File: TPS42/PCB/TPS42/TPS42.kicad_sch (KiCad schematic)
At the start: 67 parts, among them J11 Conn_01x06, J3 TP Sensor Module, J4 TP Module, J5 Conn_01x02, J7 TrackPoint, J8 Battery, J9 TP Sensor Module, SW1 SW_DPST_x2, SW2 Reset, SW3 Reset, U1 ProMicro, U11 Hole, U12 Hole, U14 ProMicro, U4 Hole, U5 Hole, U7 Hole, U8 Hole, U9 Hole

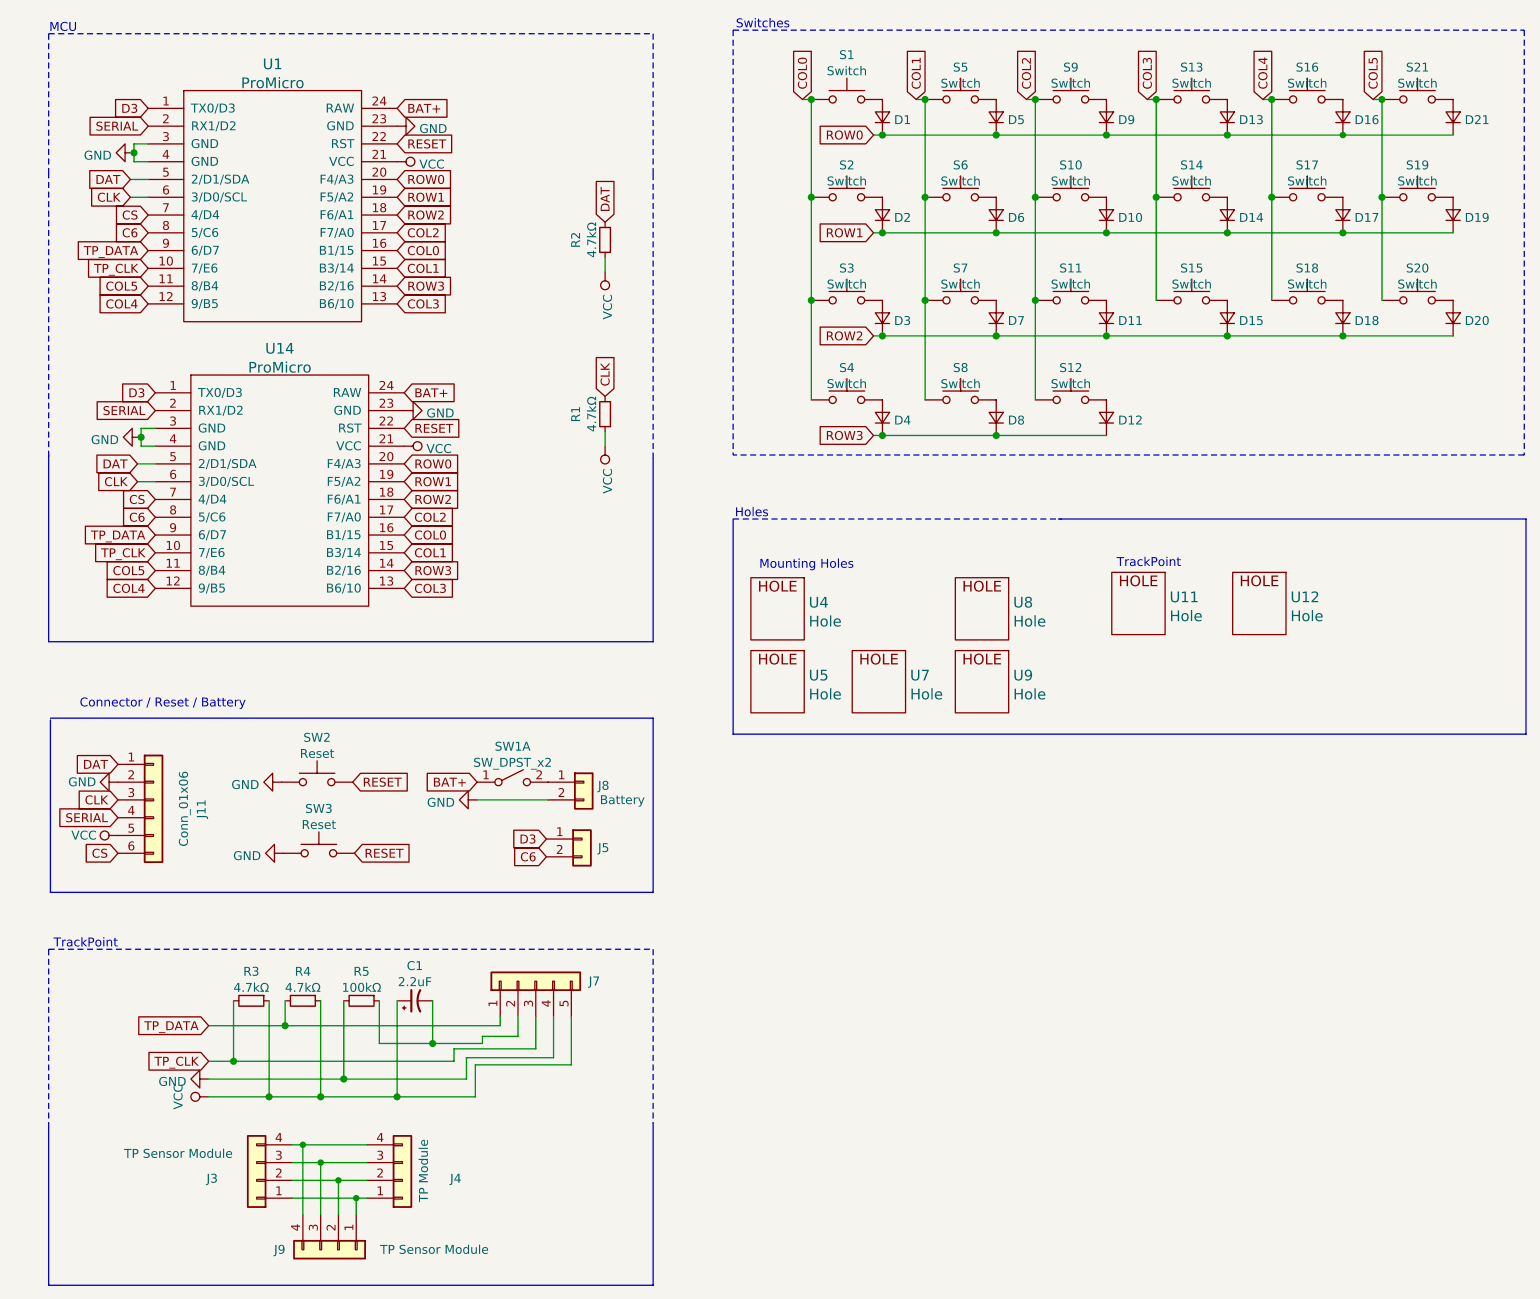
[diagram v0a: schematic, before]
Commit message: TPS42: clean up the pcb a bit, get rid of the oled/lcd shields
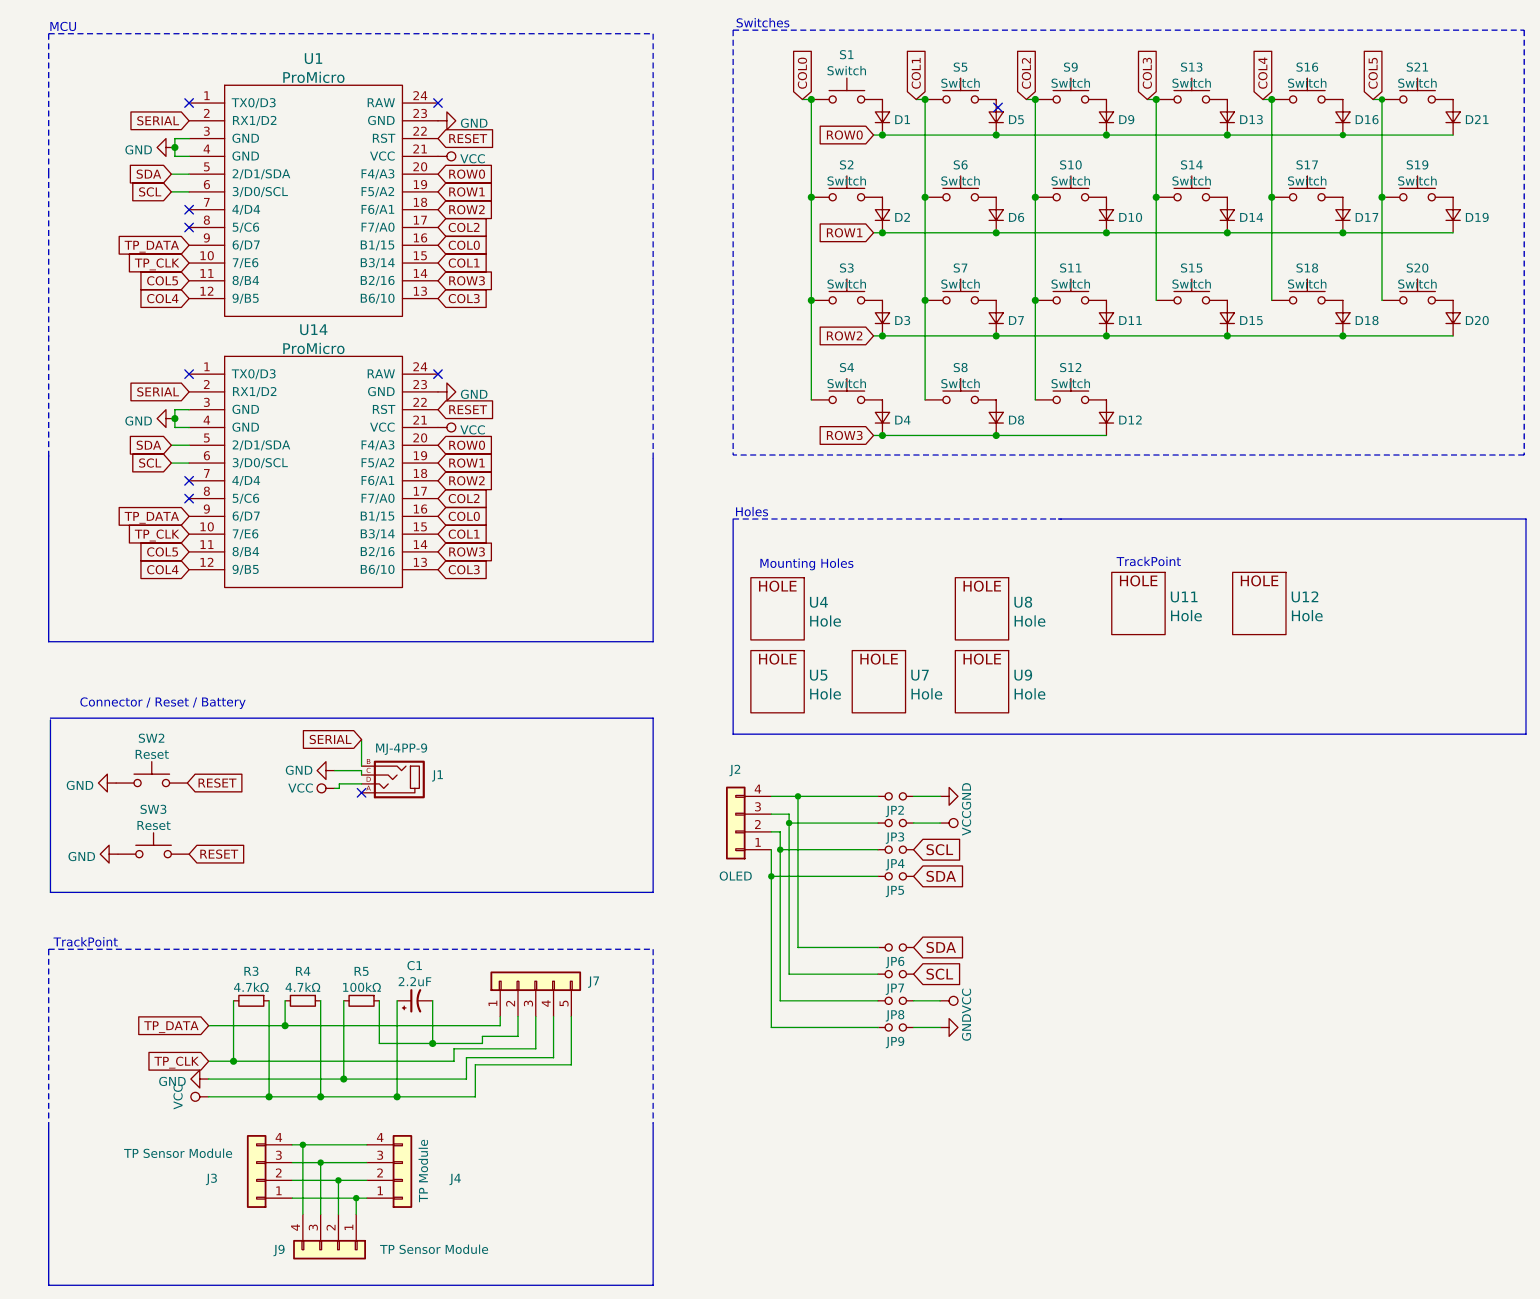
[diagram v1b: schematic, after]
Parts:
- removed J11: Conn_01x06, Connector_PinHeader_2.54mm:PinHeader_2x03_P2.54mm_Vertical, symbol Connector_Generic:Conn_01x06
- removed J5: Conn_01x02, Connector_PinHeader_2.54mm:PinHeader_1x02_P2.54mm_Vertical, symbol Connector_Generic:Conn_01x02
- removed J8: Battery, Connector_PinHeader_2.54mm:PinHeader_1x02_P2.54mm_Vertical, symbol Connector_Generic:Conn_01x02
- removed R1, R2: 4.7kΩ, TPS42:R_0603_1608Metric_Pad0.98x0.95mm_HandSolder_Reversable, symbol Device:R_Small
- removed SW1: SW_DPST_x2, TPS42:SW-TH_3P-L9.1-W3.5-P2.50-S3.20-A3, symbol Switch:SW_DPST_x2
- added J1: MJ-4PP-9, kbd:MJ-4PP-9_1side, symbol kbd:MJ-4PP-9
- added J2: OLED, kbd:OLED, symbol Connector_Generic:Conn_01x04
- added JP2, JP3, JP4, JP5, JP6, JP7, JP8, JP9: (no value), kbd:Jumper, symbol corne-chocolate-rescue:Jumper_NO_Small-Device
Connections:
- net GND: now also J1.C, JP2.1, JP9.1
- net SERIAL: now also J1.B
- net VCC: now also J1.D, JP3.1, JP8.1
- net BAT+: no longer names the net of U1.24 (RAW)
- net BAT+: no longer U14.24 (RAW)
- net C6: no longer names the net of U1.8 (5/C6)
- net C6: no longer U14.8 (5/C6)
- net CLK renamed SCL
- net SCL: now also JP4.1, JP7.1
- net CS: no longer names the net of U1.7 (4/D4)
- net CS: no longer U14.7 (4/D4)
- net D3: no longer names the net of U1.1 (TX0/D3)
- net D3: no longer U14.1 (TX0/D3)
- net DAT renamed SDA
- net SDA: now also JP5.1, JP6.1
- new net: J2.1 (Pin_1), JP5.2, JP9.2
- new net: J2.2 (Pin_2), JP4.2, JP8.2
- new net: J2.3 (Pin_3), JP3.2, JP7.2
- new net: J2.4 (Pin_4), JP2.2, JP6.2
- no-connect marks 0 -> 10
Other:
- moved on the sheet: SW2, SW3, U1, U14
